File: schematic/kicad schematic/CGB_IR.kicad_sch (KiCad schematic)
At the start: 16 parts, among them Q3 2SC4081, Q4 2SC4081, Q5 PT380F

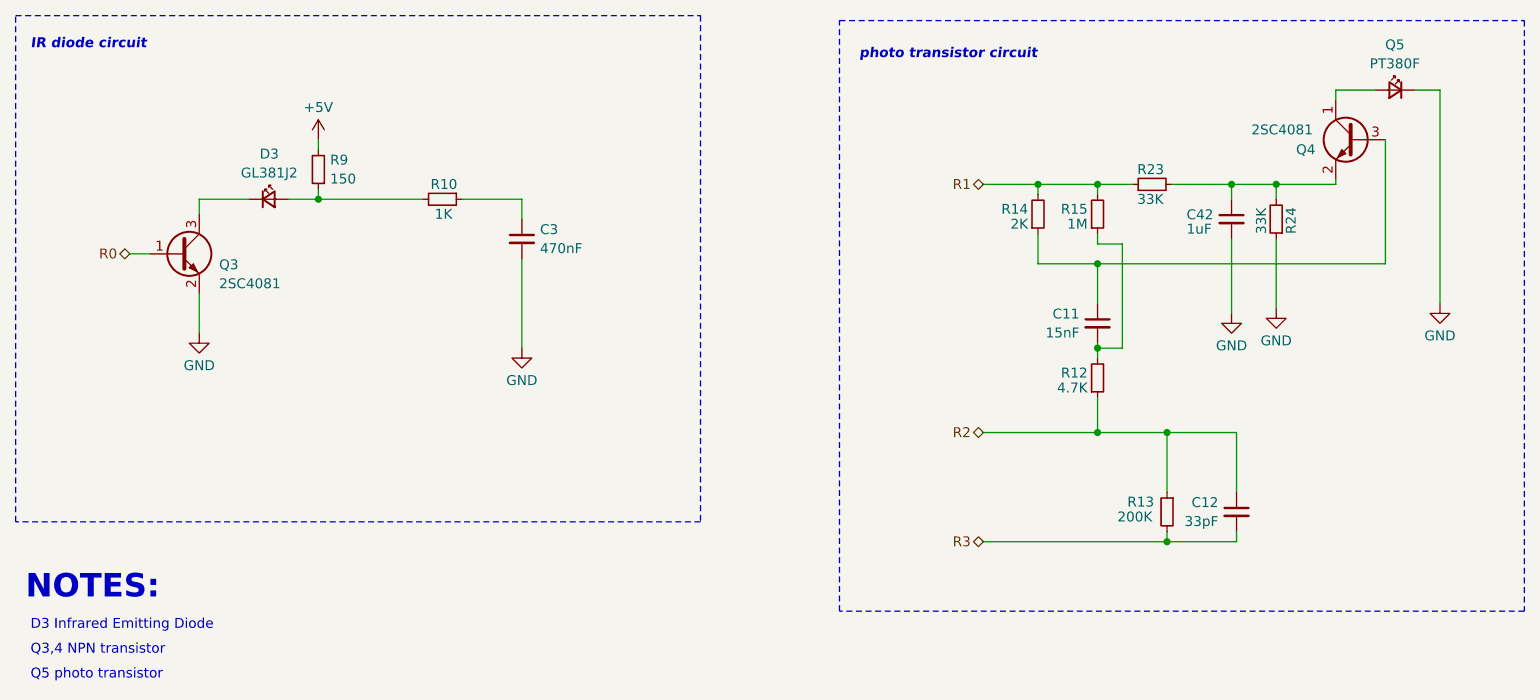
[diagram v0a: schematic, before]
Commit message: fixed schematic, thx giltesa and darren
the ir transistor was labelled wrong
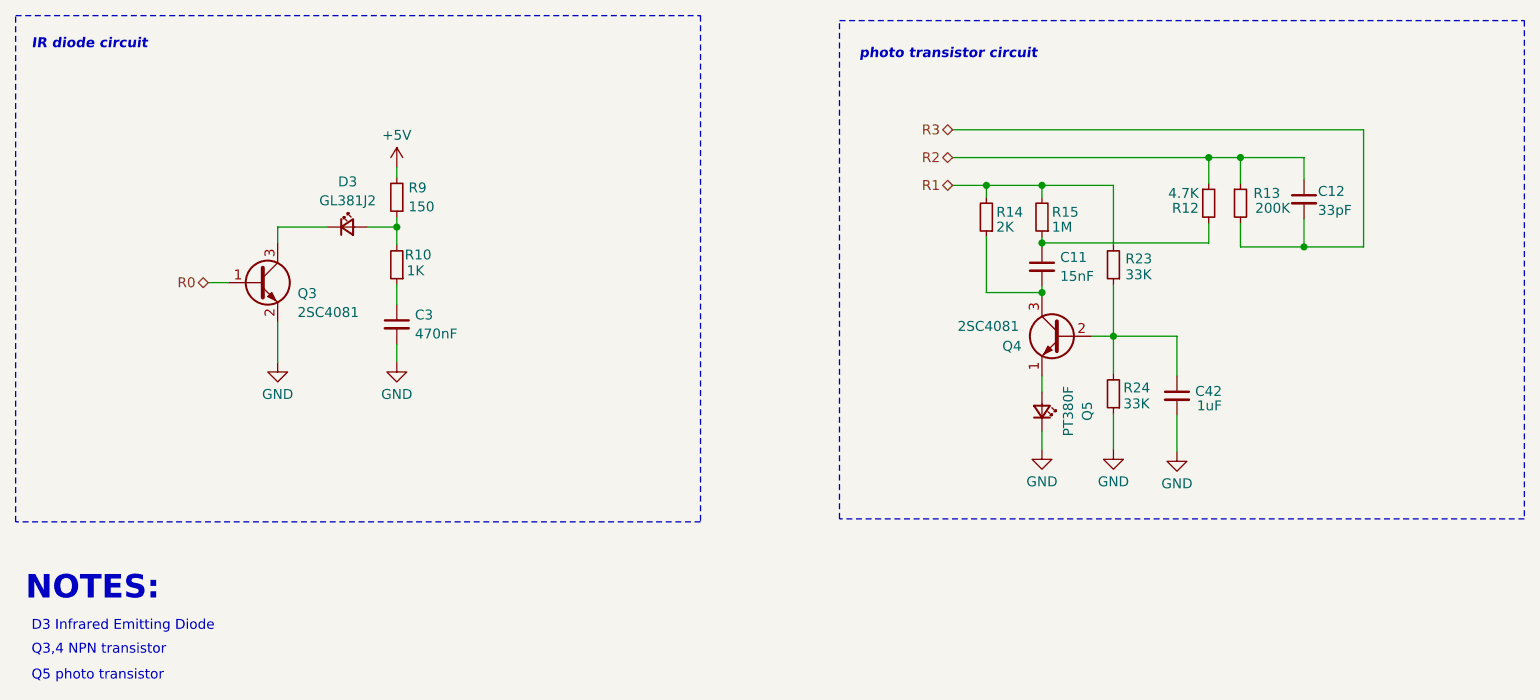
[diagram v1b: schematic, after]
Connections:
- net R1: now also R23.2; no longer R23.1
- net at Q4.3 (C), R14.1: now also C11.2; no longer C11.1
- net at R12.2, R15.1: now also C11.1; no longer C11.2
- net at C42.1, Q4.2 (B), R24.2: now also R23.1; no longer R23.2
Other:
- moved on the sheet: C11, C12, C3, C42, D3, Q3, Q4, Q5, R10, R12, R13, R15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
